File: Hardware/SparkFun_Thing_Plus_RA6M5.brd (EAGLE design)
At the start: 22.9 x 68.6 mm, 186 parts, among them J1 USB Female Type C Connector, J2 THING_PLUS_LOGICAL, J3 QWIIC_RA, J4 CONN_03X2, J7 MICRO-SDFRICTION, Q1 20V/4.2A/52mΩ/1.4W, Q2 20V/4.2A/52mΩ/1.4W, U1 R7FA6M5, U2 DA14531MOD, U3 MCP73831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

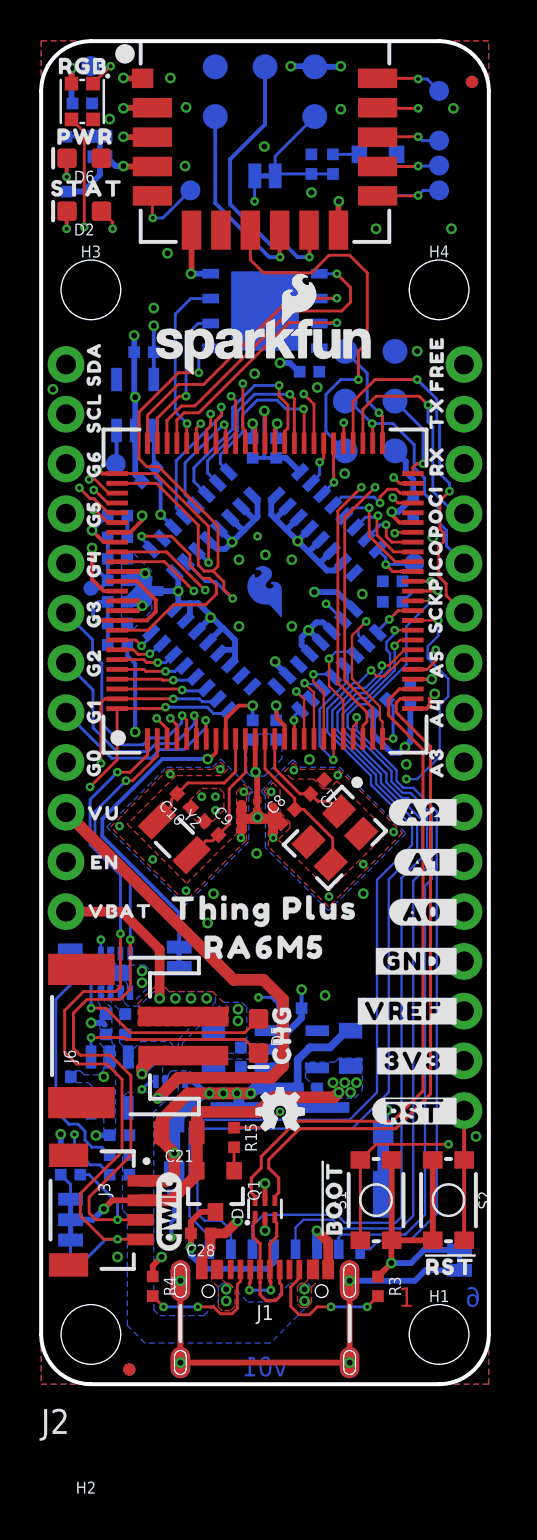
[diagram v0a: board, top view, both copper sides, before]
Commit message: Update post-design review.
Add USB diff calcs to schematic.
Add product name silk to bottom of board.
Consolidate 0.1u caps.
Stitch power and ground planes better.
Analyze PDN to chip and improve.
Pour 3V3 under USB on top and bot.
Space parts away to reduce crowding.
Increase TP sizes where possible.
Space out TPs where possible.
Space out pin silk.
Add a poly on L4 for 3V3.
Mod LM66200 sch symbol for clarity.
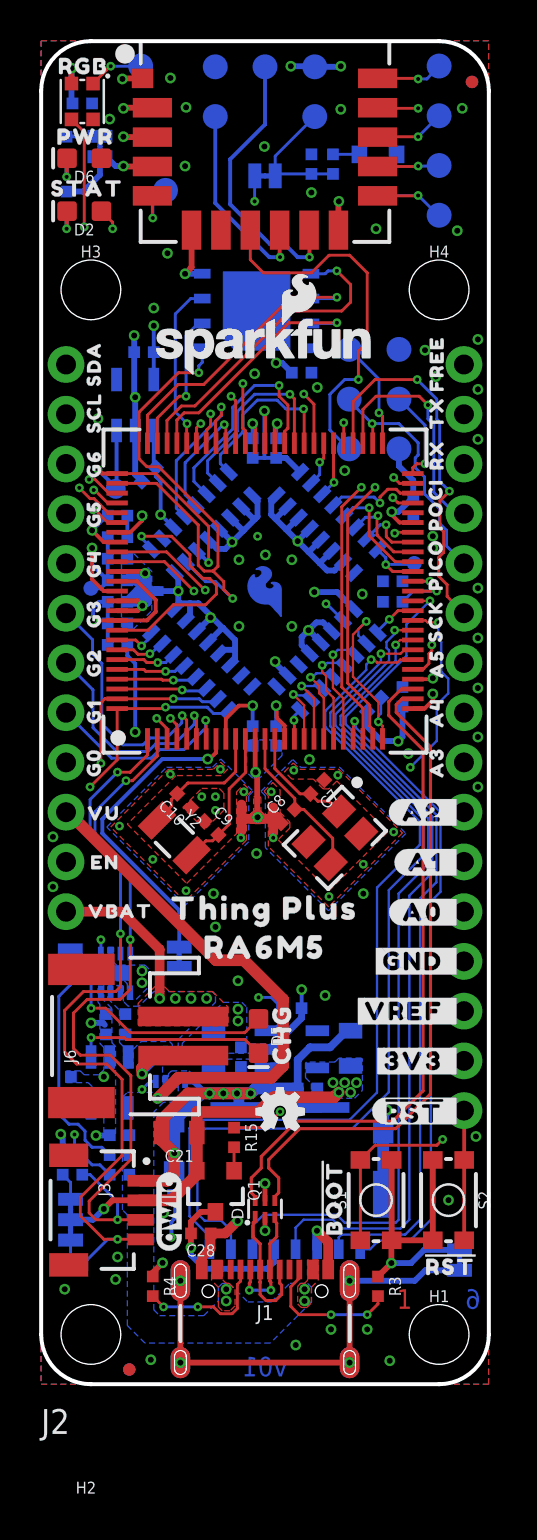
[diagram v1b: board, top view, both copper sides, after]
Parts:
- TP1, TP3, TP5, TP6, TP7, TP8: value TEST-POINT3X4 -> TEST-POINT3X5; device SparkFun-Connectors:PAD.03X.04 -> SparkFun-Connectors:PAD.03X.05
- TP9: value TEST-POINT3X4 -> TEST-POINT3; device SparkFun-Connectors:PAD.03X.04 -> SparkFun-Connectors:PAD.03X.03
- moved TP1 2.54 mm to (5.08, 67.3)
- moved TP2 1.27 mm to (3.81, 45.7)
- moved TP3 1.27 mm to (20.3, 59.7)
- moved TP6 1.27 mm to (6.35, 61.0)
- moved TP5 1.27 mm to (20.3, 64.8)
- moved TP8 1.27 mm to (20.3, 67.3)
- moved U$64 0.45 mm to (20.1, 47.5)
- moved U$29 0.45 mm to (20.1, 39.0)
- moved U$61 0.45 mm to (20.1, 39.0)
- moved U5 0.43 mm to (11.0, 54.8)
- moved C6 0.41 mm to (18.4, 35.1)
- moved C22 0.40 mm to (13.3, 51.6)
- moved U$31 0.35 mm to (20.1, 44.9)
- moved R2 0.32 mm to (17.0, 34.7)
- moved U$32 0.30 mm to (20.2, 47.5)
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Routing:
- net VREFEN: track 12.3 -> 13.9 mm
- net N$27: track 6.82 -> 5.24 mm
- net N$15: track 11.1 -> 9.67 mm
- net GND: track 157.9 -> 156.5 mm, vias 50 -> 49
- net SDDET: track 42.6 -> 41.7 mm
- net RX_RA6/TX_DA14531: track 16.9 -> 16.1 mm
- net BOOT/MD: track 73.7 -> 73.0 mm
- net QIO0: track 15.7 -> 16.3 mm
- net SDDAT1: track 33.2 -> 32.6 mm
- net RGB_DOUT: track 2.28 -> 2.80 mm
- net 3.3V: track 32.9 -> 33.3 mm, vias 37 -> 60
- added copper zone on layer 14, net 3.3V

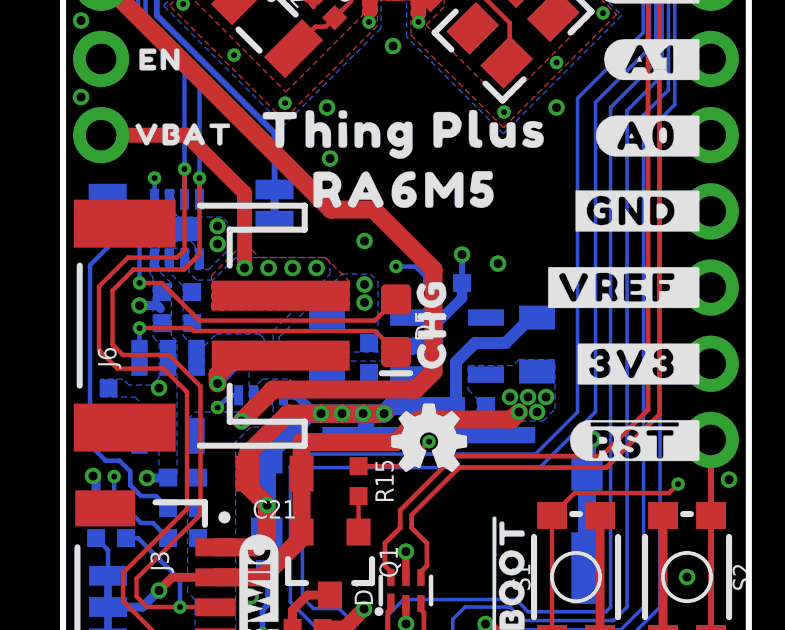
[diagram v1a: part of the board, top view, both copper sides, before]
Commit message: Minor update to v01.
Add Fuel Gauge address text to schematic.
Add +/- silk for battery connector.
Re-export PDF.
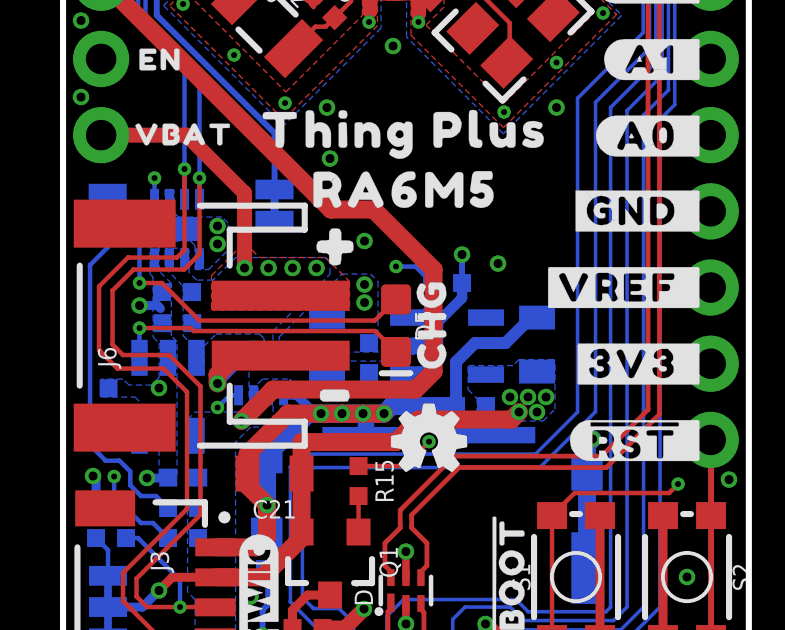
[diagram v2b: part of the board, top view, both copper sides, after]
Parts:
- added U$81: (no value), output:#0
- added U$85: (no value), output:_#0
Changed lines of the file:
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@@
 <layer number="27" name="tValues" color="7" fill="1" visible="no" active="yes"/>
 <layer number="28" name="bValues" color="7" fill="1" visible="no" active="yes"/>
-<layer number="29" name="tStop" color="7" fill="3" visible="no" active="yes"/>
-<layer number="30" name="bStop" color="7" fill="6" visible="no" active="yes"/>
+<layer number="29" name="tStop" color="7" fill="3" visible="yes" active="yes"/>
+<layer number="30" name="bStop" color="7" fill="6" visible="yes" active="yes"/>
 <layer number="31" name="tCream" color="7" fill="4" visible="no" active="yes"/>
 <layer number="32" name="bCream" color="7" fill="5" visible="no" active="yes"/>
@@
 <layer number="44" name="Drills" color="7" fill="1" visible="no" active="yes"/>
 <layer number="45" name="Holes" color="7" fill="1" visible="yes" active="yes"/>
-<layer number="46" name="Milling" color="3" fill="1" visible="no" active="yes"/>
-<layer number="47" name="Measures" color="7" fill="1" visible="no" active="yes"/>
+<layer number="46" name="Milling" color="3" fill="1" visible="yes" active="yes"/>
+<layer number="47" name="Measures" color="7" fill="1" visible="yes" active="yes"/>
 <layer number="48" name="Document" color="7" fill="1" visible="no" active="yes"/>
 <layer number="49" name="Reference" color="7" fill="1" visible="no" active="yes"/>
 <layer number="50" name="dxf" color="7" fill="1" visible="no" active="yes"/>
-<layer number="51" name="tDocu" color="6" fill="1" visible="no" active="yes"/>
+<layer number="51" name="tDocu" color="6" fill="1" visible="yes" active="yes"/>
 <layer number="52" name="bDocu" color="7" fill="1" visible="no" active="yes"/>
 <layer number="4" name="Route4" color="18" fill="1" visible="no" active="no"/>
@@
 <element name="U$83" library="output" package="THING0" value="" x="14.4" y="31.25" smashed="yes" rot="MR0"/>
 <element name="U$84" library="output" package="PLUS0" value="" x="8.35" y="31.25" smashed="yes" rot="MR0"/>
+<element name="U$81" library="output" package="#0" value="" x="9.2" y="20.4" smashed="yes"/>
+<element name="U$85" library="output" package="_#0" value="" x="8.85" y="15.45" smashed="yes"/>
 </elements>
 <signals>

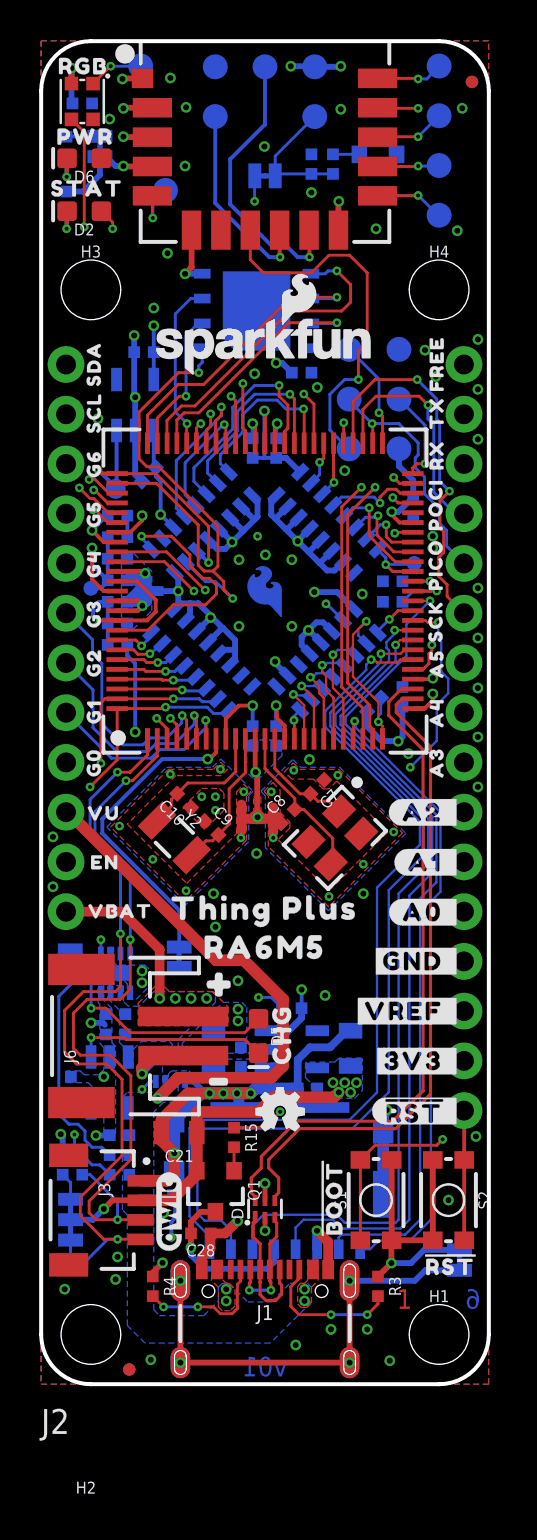
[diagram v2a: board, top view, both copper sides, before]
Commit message: Update for Reds.
Change QSPI flash chip to same one as Portenta C33
Remove boot button
Move reset button to space it out
Add boot test point
Recenter programming header silk
Update GPIO silk
Rename nets in schematic
Remove BLE Reset jumper
Remove DNP caps from 24MHz xtal
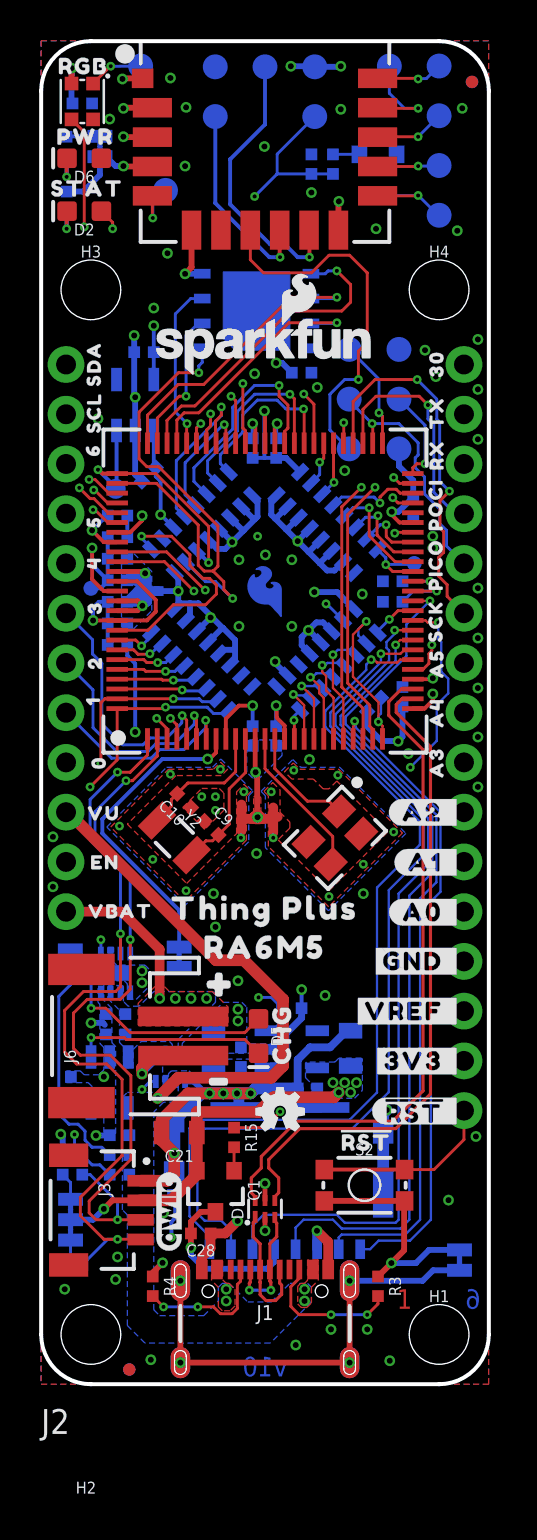
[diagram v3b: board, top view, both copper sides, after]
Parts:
- removed C7, C8: DNP, SparkFun-Capacitors:0402-TIGHT_NO_CREAM
- removed RST: JUMPER-SMT_2_NC_TRACE_SILK, SparkFun-Jumpers:SMT-JUMPER_2_NC_TRACE_SILK
- removed S1: BOOT, SparkFun-Switches:TACTILE_SWITCH_SMD_4.6X2.8MM
- removed U$73: (no value), output:G20
- removed U$74: (no value), output:#G1#0
- removed U$75: (no value), output:#G0#0
- added TP10: TEST-POINT3X5, SparkFun-Connectors:PAD.03X.05
- added U$86: (no value), output:300
- U$12: device output:#BOOT#0 -> output:300
- U$34: device output:FREE0 -> output:60
- U$37: device output:G60 -> output:50
- U$38: device output:G50 -> output:40
- U$39: device output:G40 -> output:30
- U$40: device output:G30 -> output:20
- U$41: device output:G20 -> output:10
- U$42: device output:G10 -> output:00
- U$43: device output:G00 -> output:60
- U$48: device output:##RST##0 -> output:50
- U$66: device output:FREE0 -> output:40
- U$69: device output:G60 -> output:30
- U$70: device output:G50 -> output:20
- U$71: device output:G40 -> output:#1#0
- U$72: device output:G30 -> output:#0#0
- U5: value W25QXX128MBIT-6X5 -> MX25L12833F 128Mb
- moved U$12 42.9 mm to (20.2, 52.1)
- moved U$66 20.0 mm to (2.60, 42.3)
- moved U$34 18.1 mm to (2.65, 47.7)
- moved U$48 17.4 mm to (2.60, 45.0), turned to 90 degrees
- moved U$43 15.5 mm to (2.80, 47.2), flipped to the bottom
- moved U$70 7.85 mm to (2.75, 36.8), turned to 270 degrees
- moved U$72 7.70 mm to (2.80, 31.8), turned to 0 degrees
- moved U$13 7.67 mm to (16.6, 12.4)
- moved U$71 7.60 mm to (2.70, 34.3), turned to 0 degrees
- moved U$69 7.20 mm to (2.60, 39.9)
- moved S2 4.36 mm to (16.5, 10.2), turned to 0 degrees
- moved U$37 2.95 mm to (2.70, 44.0)
- moved U$42 2.61 mm to (2.95, 31.8)
- moved U$40 2.50 mm to (2.75, 36.9)
- moved U$38 2.50 mm to (2.70, 42.0)
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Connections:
- net A0 renamed A0/DAC0/D7
- net A1 renamed A1/DAC1/D8
- net A2 renamed A2/D9
- net A3 renamed A3/D10
- net A4 renamed A4/D11
- net A5 renamed A5/D12
- net DA14531_RST renamed BLE_RST
- net FREE renamed FREE/D30
- net GPIO0/!CS! renamed GPIO0/!CS!/D0
- net GPIO1 renamed GPIO1/D1
- net GPIO2 renamed GPIO2/D2
- net GPIO3 renamed GPIO3/D3
- net GPIO4 renamed GPIO4/D4
- net GPIO5 renamed GPIO5/D5
- net GPIO6 renamed GPIO6/D6
- net RA6_SWO/TDO/PICO renamed RA6_SWO/TDO/PICO/D18
- net RA6_TDI/POCI renamed RA6_TDI/POCI/D17
- net SCK renamed SCK/D19
- net SCL renamed SCL/D16
- net SDA renamed SDA/D15
- net UART_RX renamed UART_RX/D21
- net UART_TX renamed UART_TX/D20
- removed net N$25: RST.2, U1.58
- net !DA14531_RST!: now also U1.58; no longer RST.1
- net BOOT/MD: now also TP10.1; no longer S1.3, S1.4
- net EXTAL: no longer C7.2
- net GND: no longer S1.1, S1.2
- net GND_24: no longer C7.1, C8.1
- net XTAL: no longer C8.2
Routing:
- net BOOT/MD: track 73.0 -> 37.8 mm, vias 3 -> 2
- net !DA14531_RST!: track 6.86 -> 22.4 mm, vias 0 -> 2
- net N$25: track 15.3 -> 0.00 mm, vias 2 -> 0
- net GND: track 156.5 -> 152.6 mm
- net !RA6M5_RESET!: track 70.9 -> 73.5 mm
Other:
- board text added: "v10"
- board text removed: "v01"

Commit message: V10 hardware post reds review update
Connect fills on bottom side near bottom diamond.
Add user button near reset button.
VREF EN now pulls up to 3.3V instead of VIN.
Change VREF silk bottom side to inverted VA.
Update EN and !RST! silk flags to use the right arrow.
Move vias to allow fills.
Adjust guard trace around Y1 to accommodate removing caps.
Add ground vias near QSPI data lines where possible.
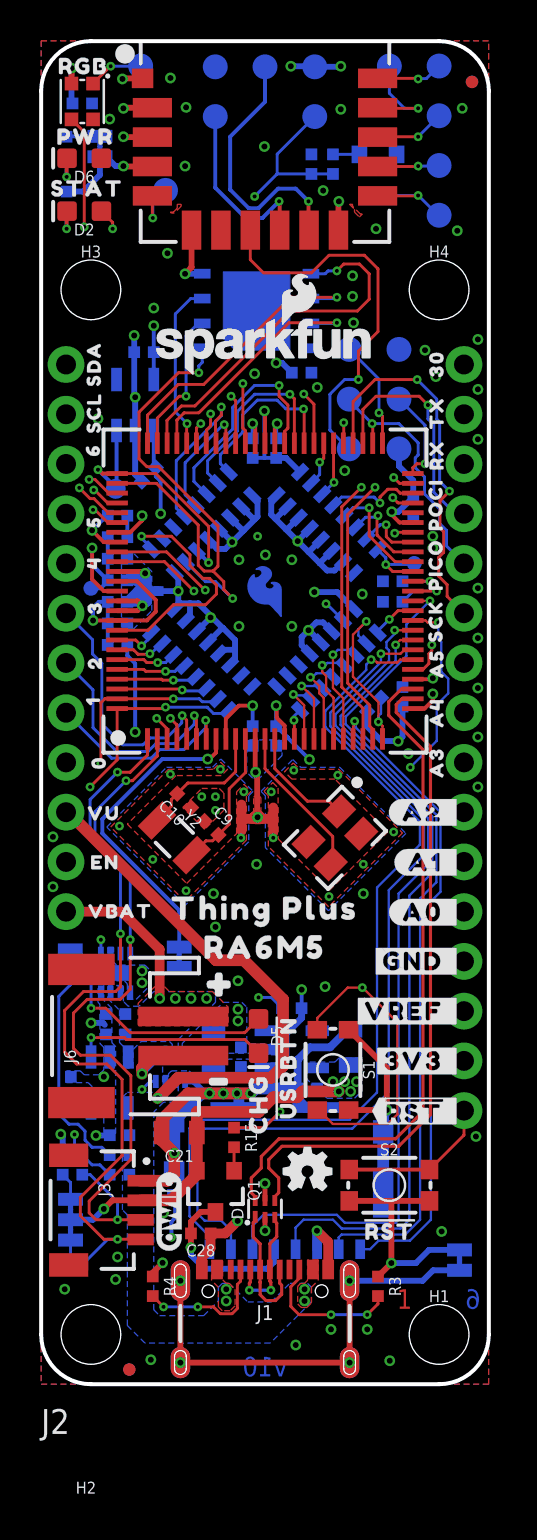
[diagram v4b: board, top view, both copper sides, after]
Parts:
- added S1: USER, SparkFun-Switches:TACTILE_SWITCH_SMD_4.6X2.8MM
- added U$73: (no value), output:#USRBTN#0
- U$53: device output:VREF0 -> output:#_VA#0
- moved U$13 4.71 mm to (17.8, 7.90)
- moved U$14 3.75 mm to (11.1, 14.3)
- moved LOGO1 3.36 mm to (13.6, 10.9)
- moved U$53 2.60 mm to (21.4, 19.1)
- moved S2 1.27 mm to (17.8, 10.2)
- moved C24 0.05 mm to (15.8, 17.2)
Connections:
- removed net N$12: RN3.15, U1.17
- new net !USR_BTN!: RN3.15, S1.1, S1.2, U1.17
- net 3.3V: now also RN1.11, RN3.2
- net GND: now also S1.3, S1.4; no longer RN3.2
- net VIN: no longer RN1.11
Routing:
- net !USR_BTN!: track 0.00 -> 38.6 mm, vias 0 -> 2
- net GND: track 152.6 -> 158.2 mm, vias 49 -> 51
- net N$12: track 3.51 -> 0.00 mm, vias 1 -> 0
- net QIO0: track 16.3 -> 18.7 mm
- net 3.3V: track 33.3 -> 35.7 mm
- net VIN: track 49.3 -> 48.3 mm
- net DA14531_SWDIO: track 10.3 -> 9.37 mm
- net DA14531_SWCLK: track 14.3 -> 13.6 mm
- net USBD_P: track 34.3 -> 34.9 mm
- net USBD_N: track 33.6 -> 34.2 mm
- net !CTS_RA6/RTS_DA14531!: track 24.4 -> 24.9 mm
- net !RA6M5_RESET!: track 73.5 -> 73.0 mm

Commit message: Rename silk
VA to VR.
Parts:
- U$53: device output:#_VA#0 -> output:#_VR#0
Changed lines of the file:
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@@
 </element>
 <element name="U$73" library="output" package="#USRBTN#0" value="" x="12.5" y="16.15" smashed="yes" rot="R90"/>
-<element name="U$53" library="output" package="#_VA#0" value="" x="21.45" y="19.05" smashed="yes" rot="MR0"/>
+<element name="U$53" library="output" package="#_VR#0" value="" x="21.45" y="19.05" smashed="yes" rot="MR0"/>
 </elements>
 <signals>
